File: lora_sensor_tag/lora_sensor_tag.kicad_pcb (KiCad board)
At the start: 4 copper layers, 55.4 x 63.3 mm, 150 parts, among them J1 Conn_Coaxial, J2 Conn_Coaxial, J3 Li-ion_bat_conn, J4 USB_C_Receptacle_USB2.0_14P, Q1 NPN, Q2 NPN, Q3 NPN, SW1 SW_MCU_RST, SW2 SW_MCU_PROG, U1 SX1276IMLTRT, U2 ESP32-WROOM-32D, U3 PE4259, U4 SHT20, U5 TPS63070RNMR, U6 MCP73871-2CAI_ML, U7 AMS1117-3.3, U8 MAX17048G_T10, U9 CP2102N-Axx-xQFN28, Y1 32 MHz

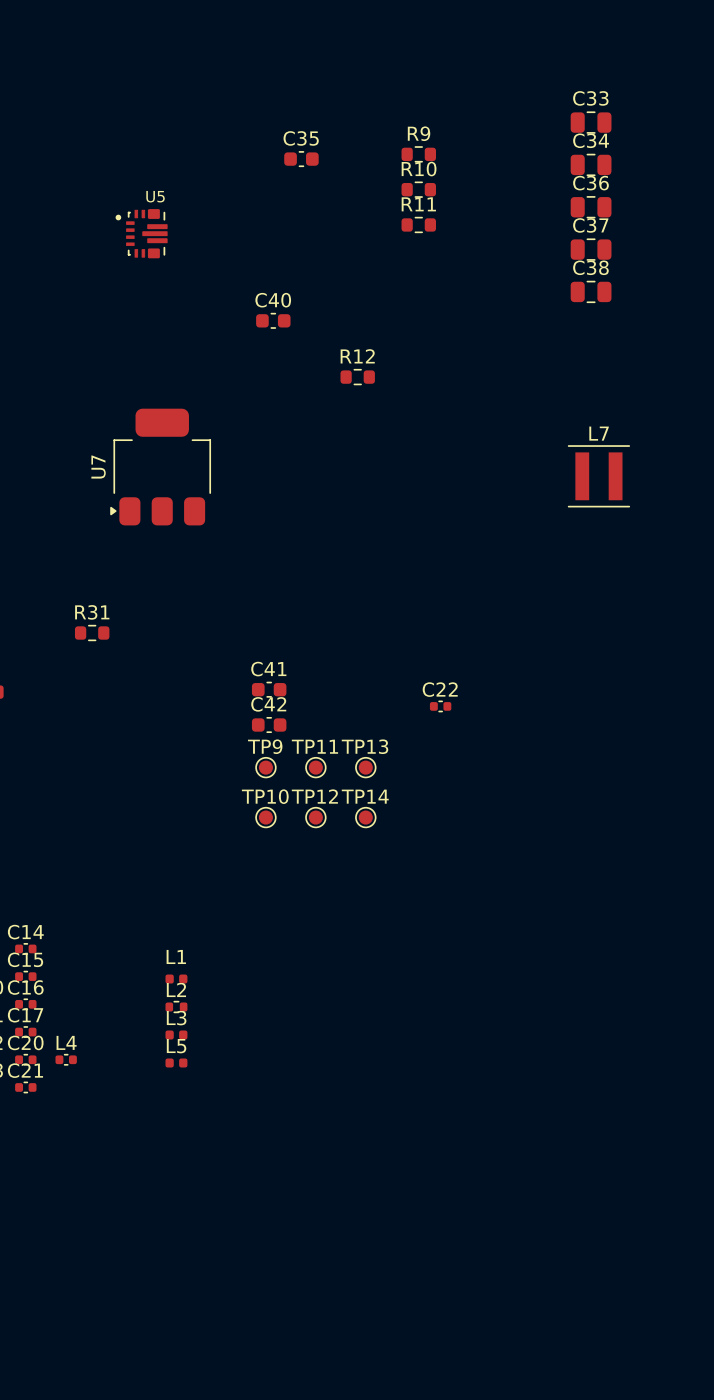
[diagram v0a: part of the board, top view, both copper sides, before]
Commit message: DC-DC buckboost to 3V3 using TPS63060.
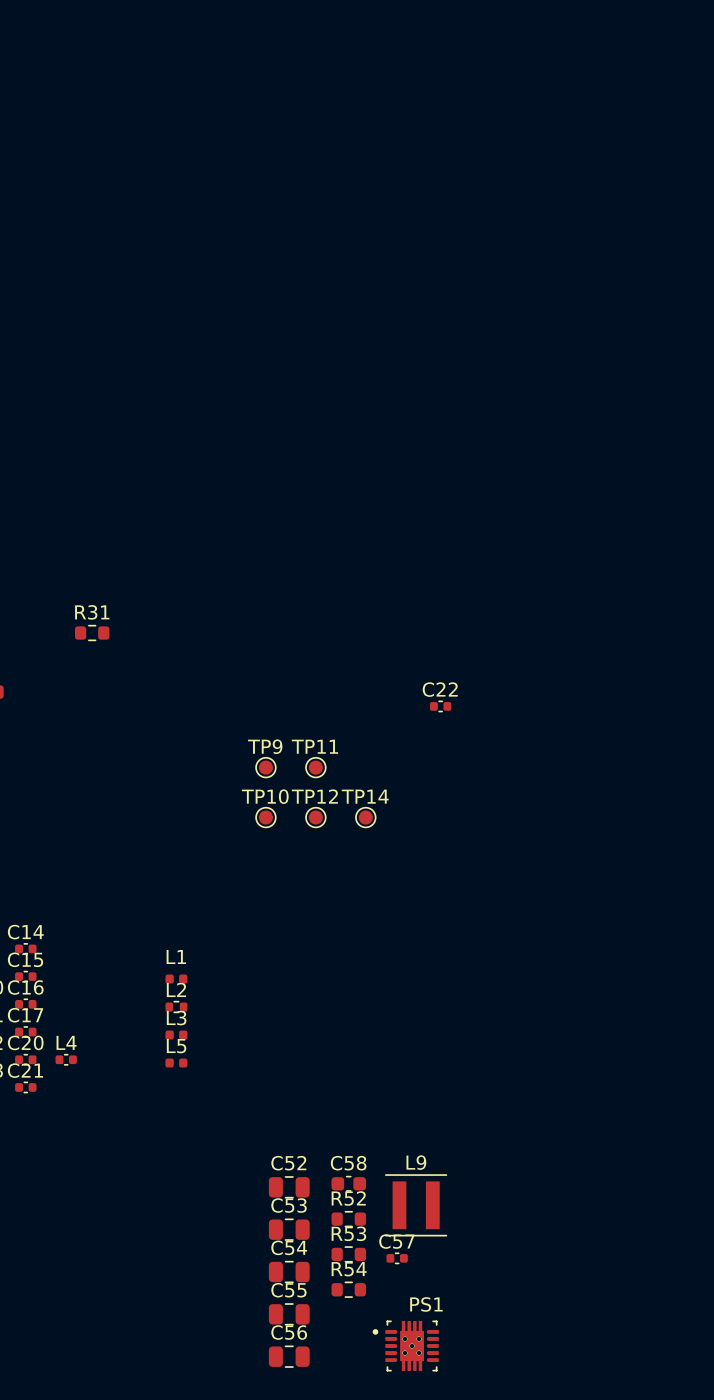
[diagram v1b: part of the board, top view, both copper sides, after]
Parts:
- removed C33, C34: 10uF, Capacitor_SMD:C_0805_2012Metric
- removed C35, C41: 10uF, Capacitor_SMD:C_0603_1608Metric
- removed C36, C37, C38: 22uF, Capacitor_SMD:C_0805_2012Metric
- removed C40: 100nF, Capacitor_SMD:C_0603_1608Metric
- removed C42: 22uF, Capacitor_SMD:C_0603_1608Metric
- removed L7: 1.5uH, Inductor_SMD:L_Coilcraft_XxL4040
- removed R10: 680K, Resistor_SMD:R_0603_1608Metric
- removed R11: 10K, Resistor_SMD:R_0603_1608Metric
- removed R12: 130K, Resistor_SMD:R_0603_1608Metric
- removed R9: R, Resistor_SMD:R_0603_1608Metric
- removed TP13: TestPoint, TestPoint:TestPoint_Pad_D1.0mm
- removed U5: TPS63070RNMR, TPS63070RNMR:VREG_TPS63070RNMR
- removed U7: AMS1117-3.3, Package_TO_SOT_SMD:SOT-223-3_TabPin2
- added C52: 22uF, Capacitor_SMD:C_0805_2012Metric, F.Cu at (62.8, 151.2)
- added C53: 22uF, Capacitor_SMD:C_0805_2012Metric, F.Cu at (62.8, 154.2)
- added C54: 22uF, Capacitor_SMD:C_0805_2012Metric, F.Cu at (62.8, 157.2)
- added C55: 10uF, Capacitor_SMD:C_0805_2012Metric, F.Cu at (62.8, 160.2)
- added C56: 10uF, Capacitor_SMD:C_0805_2012Metric, F.Cu at (62.8, 163.3)
- added C57: 100nF, Capacitor_SMD:C_0402_1005Metric, F.Cu at (70.4, 156.3)
- added C58: 10pF, Capacitor_SMD:C_0603_1608Metric, F.Cu at (67.0, 151.0)
- added L9: 1uH, Inductor_SMD:L_Coilcraft_XxL4020, F.Cu at (71.8, 152.5)
- added PS1: TPS63060DSCR, TPS63060DSCR:CONV_TPS63060DSCR, F.Cu at (71.5, 162.5)
- added R52: 560K, Resistor_SMD:R_0603_1608Metric, F.Cu at (67.0, 153.5)
- added R53: 100K, Resistor_SMD:R_0603_1608Metric, F.Cu at (67.0, 156.0)
- added R54: 1M, Resistor_SMD:R_0603_1608Metric, F.Cu at (67.0, 158.5)
